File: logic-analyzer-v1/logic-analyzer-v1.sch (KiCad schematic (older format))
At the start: 0 parts

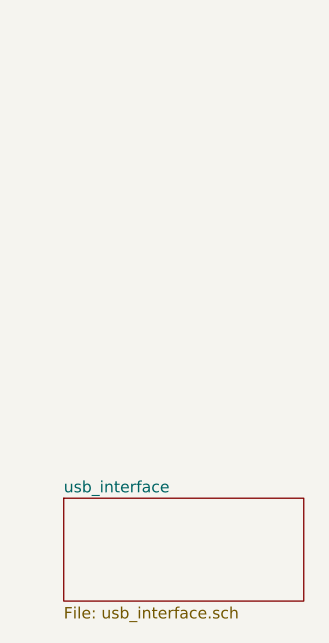
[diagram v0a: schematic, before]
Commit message: MOD usb-interface - review and minor fixes
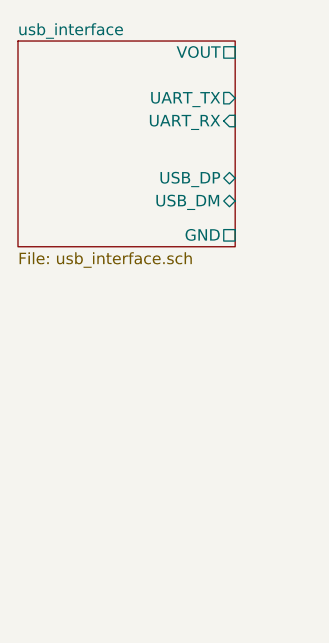
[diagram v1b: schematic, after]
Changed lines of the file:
@@
 $EndDescr
 $Sheet
-S 1350 5150 1050 450
+S 1150 3150 950  900
 U 5F08ED8D
 F0 "usb_interface" 50
 F1 "usb_interface.sch" 50
+F2 "UART_TX" O R 2100 3400 50
+F3 "UART_RX" I R 2100 3500 50
+F4 "VOUT" U R 2100 3200 50
+F5 "GND" U R 2100 4000 50
+F6 "USB_DP" B R 2100 3750 50
+F7 "USB_DM" B R 2100 3850 50
 $EndSheet
 $EndSCHEMATC

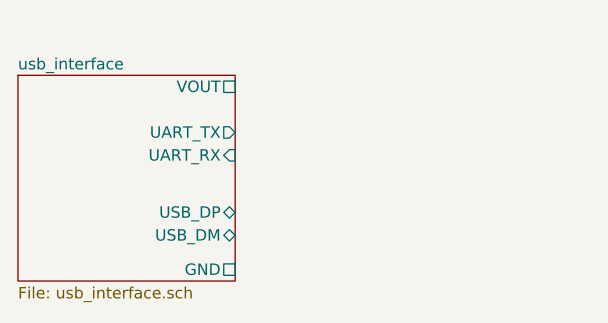
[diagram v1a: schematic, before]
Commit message: modify mcu sheet -> adding front end
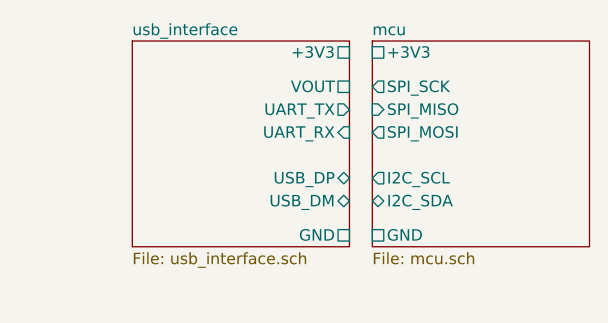
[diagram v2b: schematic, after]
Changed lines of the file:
@@
 $Descr A4 11693 8268
 encoding utf-8
-Sheet 1 2
+Sheet 1 3
 Title ""
 Date ""
@@
 $EndDescr
 $Sheet
-S 1150 3150 950  900
+S 1650 3000 950  900
 U 5F08ED8D
 F0 "usb_interface" 50
 F1 "usb_interface.sch" 50
-F2 "UART_TX" O R 2100 3400 50
-F3 "UART_RX" I R 2100 3500 50
-F4 "VOUT" U R 2100 3200 50
-F5 "GND" U R 2100 4000 50
-F6 "USB_DP" B R 2100 3750 50
-F7 "USB_DM" B R 2100 3850 50
+F2 "UART_TX" O R 2600 3300 50
+F3 "UART_RX" I R 2600 3400 50
+F4 "VOUT" U R 2600 3200 50
+F5 "GND" U R 2600 3850 50
+F6 "USB_DP" B R 2600 3600 50
+F7 "USB_DM" B R 2600 3700 50
+F8 "+3V3" U R 2600 3050 50
+$EndSheet
+$Sheet
+S 2700 3000 950  900
+U 5F19654C
+F0 "mcu" 50
+F1 "mcu.sch" 50
+F2 "I2C_SCL" O L 2700 3600 50
+F3 "I2C_SDA" B L 2700 3700 50
+F4 "SPI_MOSI" O L 2700 3400 50
+F5 "SPI_MISO" I L 2700 3300 50
+F6 "SPI_SCK" O L 2700 3200 50
+F7 "+3V3" U L 2700 3050 50
+F8 "GND" U L 2700 3850 50
 $EndSheet
 $EndSCHEMATC

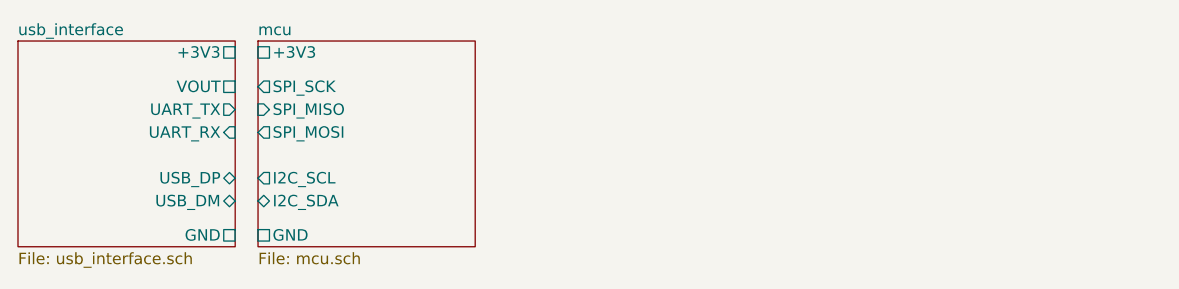
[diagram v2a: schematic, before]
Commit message: MOD usb power nets fix, mcu fixes
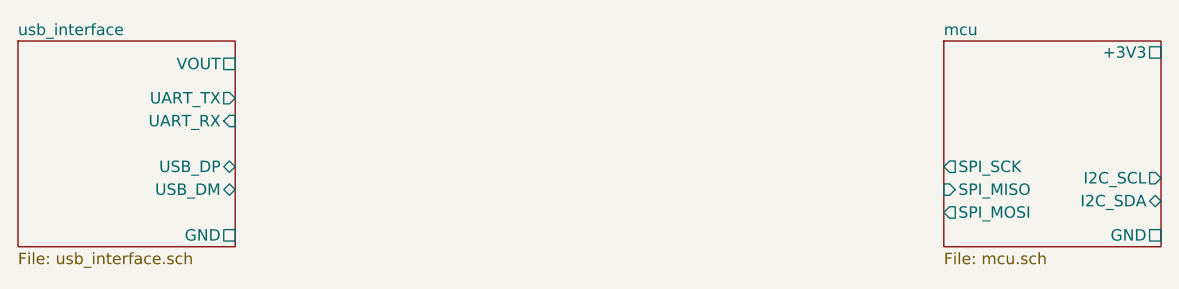
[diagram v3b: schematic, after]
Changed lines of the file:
@@
 F0 "usb_interface" 50
 F1 "usb_interface.sch" 50
-F2 "UART_TX" O R 2600 3300 50
-F3 "UART_RX" I R 2600 3400 50
-F4 "VOUT" U R 2600 3200 50
+F2 "UART_TX" O R 2600 3250 50
+F3 "UART_RX" I R 2600 3350 50
+F4 "VOUT" U R 2600 3100 50
 F5 "GND" U R 2600 3850 50
-F6 "USB_DP" B R 2600 3600 50
-F7 "USB_DM" B R 2600 3700 50
-F8 "+3V3" U R 2600 3050 50
+F6 "USB_DP" B R 2600 3550 50
+F7 "USB_DM" B R 2600 3650 50
 $EndSheet
 $Sheet
-S 2700 3000 950  900
+S 5700 3000 950  900
 U 5F19654C
 F0 "mcu" 50
 F1 "mcu.sch" 50
-F2 "I2C_SCL" O L 2700 3600 50
-F3 "I2C_SDA" B L 2700 3700 50
-F4 "SPI_MOSI" O L 2700 3400 50
-F5 "SPI_MISO" I L 2700 3300 50
-F6 "SPI_SCK" O L 2700 3200 50
-F7 "+3V3" U L 2700 3050 50
-F8 "GND" U L 2700 3850 50
+F2 "I2C_SCL" O R 6650 3600 50
+F3 "I2C_SDA" B R 6650 3700 50
+F4 "SPI_MOSI" O L 5700 3750 50
+F5 "SPI_MISO" I L 5700 3650 50
+F6 "SPI_SCK" O L 5700 3550 50
+F7 "+3V3" U R 6650 3050 50
+F8 "GND" U R 6650 3850 50
 $EndSheet
 $EndSCHEMATC

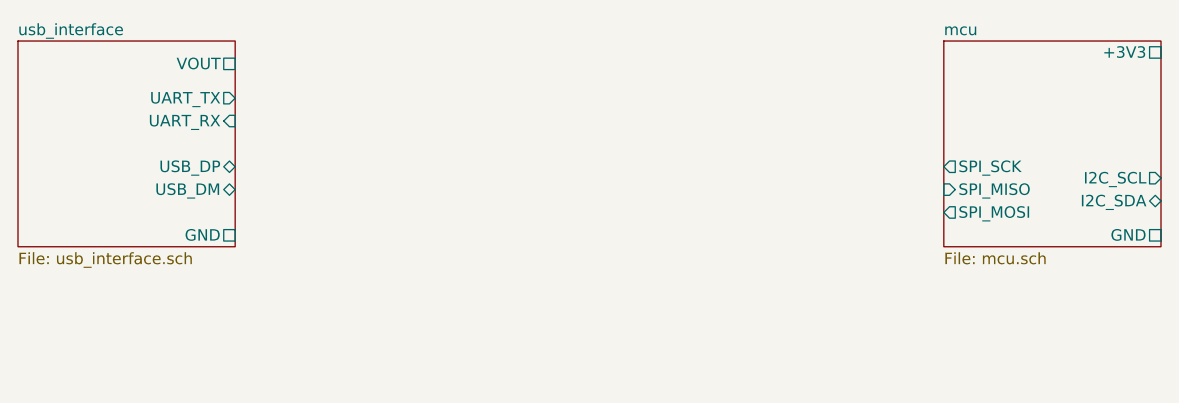
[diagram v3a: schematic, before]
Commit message: adding gpio pins, usb pins, usart pins
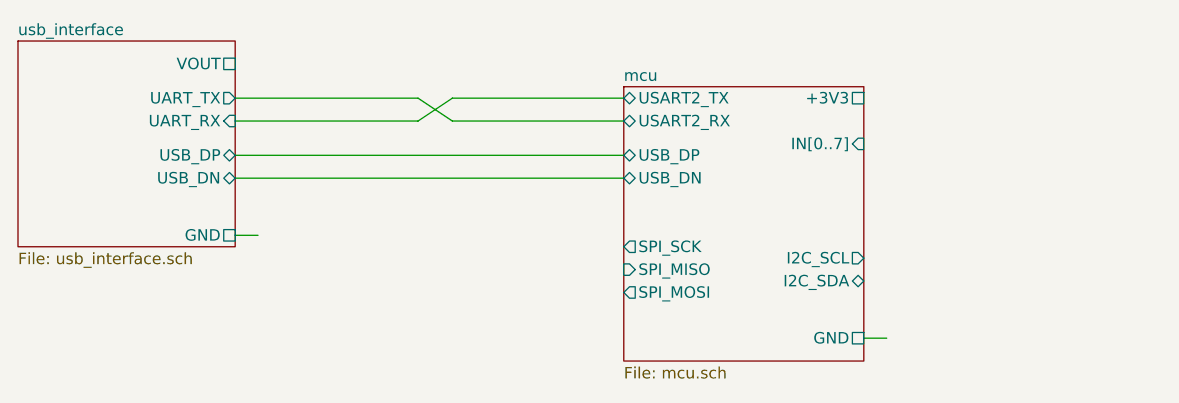
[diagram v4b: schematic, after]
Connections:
- wire segments 0 -> 10
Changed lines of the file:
@@
 F4 "VOUT" U R 2600 3100 50
 F5 "GND" U R 2600 3850 50
-F6 "USB_DP" B R 2600 3550 50
-F7 "USB_DM" B R 2600 3650 50
+F6 "USB_DP" B R 2600 3500 50
+F7 "USB_DN" B R 2600 3600 50
 $EndSheet
 $Sheet
-S 5700 3000 950  900
+S 4300 3200 1050 1200
 U 5F19654C
 F0 "mcu" 50
 F1 "mcu.sch" 50
-F2 "I2C_SCL" O R 6650 3600 50
-F3 "I2C_SDA" B R 6650 3700 50
-F4 "SPI_MOSI" O L 5700 3750 50
-F5 "SPI_MISO" I L 5700 3650 50
-F6 "SPI_SCK" O L 5700 3550 50
-F7 "+3V3" U R 6650 3050 50
-F8 "GND" U R 6650 3850 50
+F2 "I2C_SCL" O R 5350 3950 50
+F3 "I2C_SDA" B R 5350 4050 50
+F4 "SPI_MOSI" O L 4300 4100 50
+F5 "SPI_MISO" I L 4300 4000 50
+F6 "SPI_SCK" O L 4300 3900 50
+F7 "+3V3" U R 5350 3250 50
+F8 "GND" U R 5350 4300 50
+F9 "IN[0..7]" I R 5350 3450 50
+F10 "USB_DN" B L 4300 3600 50
+F11 "USB_DP" B L 4300 3500 50
+F12 "USART2_TX" B L 4300 3250 50
+F13 "USART2_RX" B L 4300 3350 50
 $EndSheet
+Wire Wire Line
+	2600 3250 3400 3250
+Wire Wire Line
+	4300 3350 3550 3350
+Wire Wire Line
+	3550 3350 3400 3250
+Wire Wire Line
+	4300 3250 3550 3250
+Wire Wire Line
+	3550 3250 3400 3350
+Wire Wire Line
+	3400 3350 2600 3350
+Wire Wire Line
+	2600 3500 4300 3500
+Wire Wire Line
+	4300 3600 2600 3600
+Wire Wire Line
+	5350 4300 5450 4300
+Wire Wire Line
+	2700 3850 2600 3850
 $EndSCHEMATC

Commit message: update 03.2021
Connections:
- wire segments 10 -> 27
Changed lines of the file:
@@
 $Descr A4 11693 8268
 encoding utf-8
-Sheet 1 3
+Sheet 1 6
 Title ""
 Date ""
@@
 F7 "USB_DN" B R 2600 3600 50
 $EndSheet
-$Sheet
-S 4300 3200 1050 1200
-U 5F19654C
-F0 "mcu" 50
-F1 "mcu.sch" 50
-F2 "I2C_SCL" O R 5350 3950 50
-F3 "I2C_SDA" B R 5350 4050 50
-F4 "SPI_MOSI" O L 4300 4100 50
-F5 "SPI_MISO" I L 4300 4000 50
-F6 "SPI_SCK" O L 4300 3900 50
-F7 "+3V3" U R 5350 3250 50
-F8 "GND" U R 5350 4300 50
-F9 "IN[0..7]" I R 5350 3450 50
-F10 "USB_DN" B L 4300 3600 50
-F11 "USB_DP" B L 4300 3500 50
-F12 "USART2_TX" B L 4300 3250 50
-F13 "USART2_RX" B L 4300 3350 50
-$EndSheet
 Wire Wire Line
 	2600 3250 3400 3250
@@
 Wire Wire Line
 	2700 3850 2600 3850
+$Sheet
+S 5950 3200 1100 1200
+U 5FDA887A
+F0 "frontend" 50
+F1 "frontend.sch" 50
+F2 "GND" U L 5950 4300 50
+F3 "I2C_SCL" I L 5950 3950 50
+F4 "I2C_SDA" B L 5950 4050 50
+$EndSheet
+Wire Wire Line
+	5950 3950 5350 3950
+Wire Wire Line
+	5350 4050 5950 4050
+$Sheet
+S 1800 4400 800  950
+U 5FDBE2FD
+F0 "memory" 50
+F1 "memory.sch" 50
+F2 "SPI_MOSI" I R 2600 4850 50
+F3 "SPI_MISO" O R 2600 4750 50
+F4 "SPI_SCK" I R 2600 4650 50
+F5 "SPI_CS_0" I R 2600 5050 50
+F6 "SPI_CS_1" I R 2600 5150 50
+F7 "GND" U R 2600 5300 50
+F8 "+3V3" U R 2600 4450 50
+$EndSheet
+$Sheet
+S 4300 3200 1050 1200
+U 5F19654C
+F0 "mcu" 50
+F1 "mcu.sch" 50
+F2 "I2C_SCL" O R 5350 3950 50
+F3 "I2C_SDA" B R 5350 4050 50
+F4 "SPI_MOSI" O L 4300 4000 50
+F5 "SPI_MISO" I L 4300 3900 50
+F6 "SPI_SCK" O L 4300 3800 50
+F7 "+3V3" U R 5350 3250 50
+F8 "GND" U R 5350 4300 50
+F9 "IN[0..7]" I R 5350 3450 50
+F10 "USB_DN" B L 4300 3600 50
+F11 "USB_DP" B L 4300 3500 50
+F12 "USART2_TX" B L 4300 3250 50
+F13 "USART2_RX" B L 4300 3350 50
+F14 "SPI_CS_0" O L 4300 4200 50
+F15 "SPI_CS_1" O L 4300 4300 50
+$EndSheet
+Wire Wire Line
+	4300 3800 3400 3800
+Wire Wire Line
+	3400 3800 3400 4650
+Wire Wire Line
+	3400 4650 2600 4650
+Wire Wire Line
+	4300 3900 3500 3900
+Wire Wire Line
+	3500 3900 3500 4750
+Wire Wire Line
+	3500 4750 2600 4750
+Wire Wire Line
+	4300 4000 3600 4000
+Wire Wire Line
+	3600 4000 3600 4850
+Wire Wire Line
+	3600 4850 2600 4850
+Wire Wire Line
+	4300 4200 3800 4200
+Wire Wire Line
+	3800 4200 3800 5050
+Wire Wire Line
+	3800 5050 2600 5050
+Wire Wire Line
+	4300 4300 3900 4300
+Wire Wire Line
+	3900 4300 3900 5150
+Wire Wire Line
+	3900 5150 2600 5150
 $EndSCHEMATC

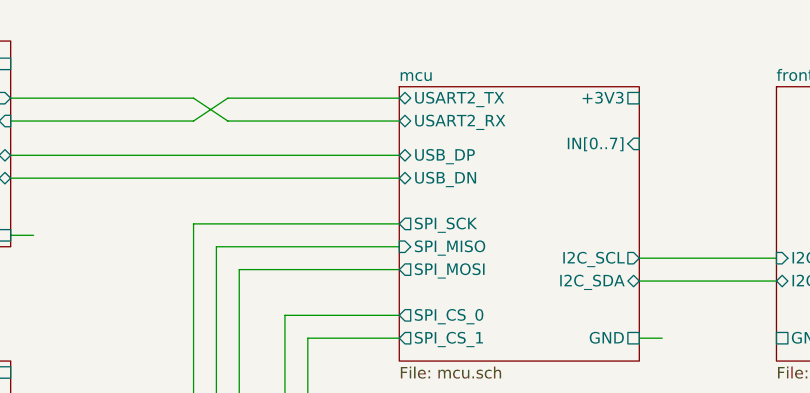
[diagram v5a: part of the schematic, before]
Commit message: MOD uart port direction, minor cosmetic changes
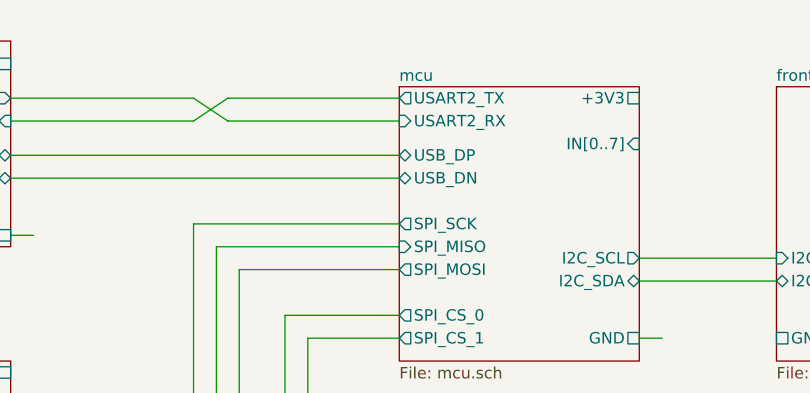
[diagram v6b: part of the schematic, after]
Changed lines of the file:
@@
 $Descr A4 11693 8268
 encoding utf-8
-Sheet 1 6
+Sheet 1 8
 Title ""
 Date ""
@@
 F10 "USB_DN" B L 4300 3600 50
 F11 "USB_DP" B L 4300 3500 50
-F12 "USART2_TX" B L 4300 3250 50
-F13 "USART2_RX" B L 4300 3350 50
+F12 "USART2_TX" O L 4300 3250 50
+F13 "USART2_RX" I L 4300 3350 50
 F14 "SPI_CS_0" O L 4300 4200 50
 F15 "SPI_CS_1" O L 4300 4300 50

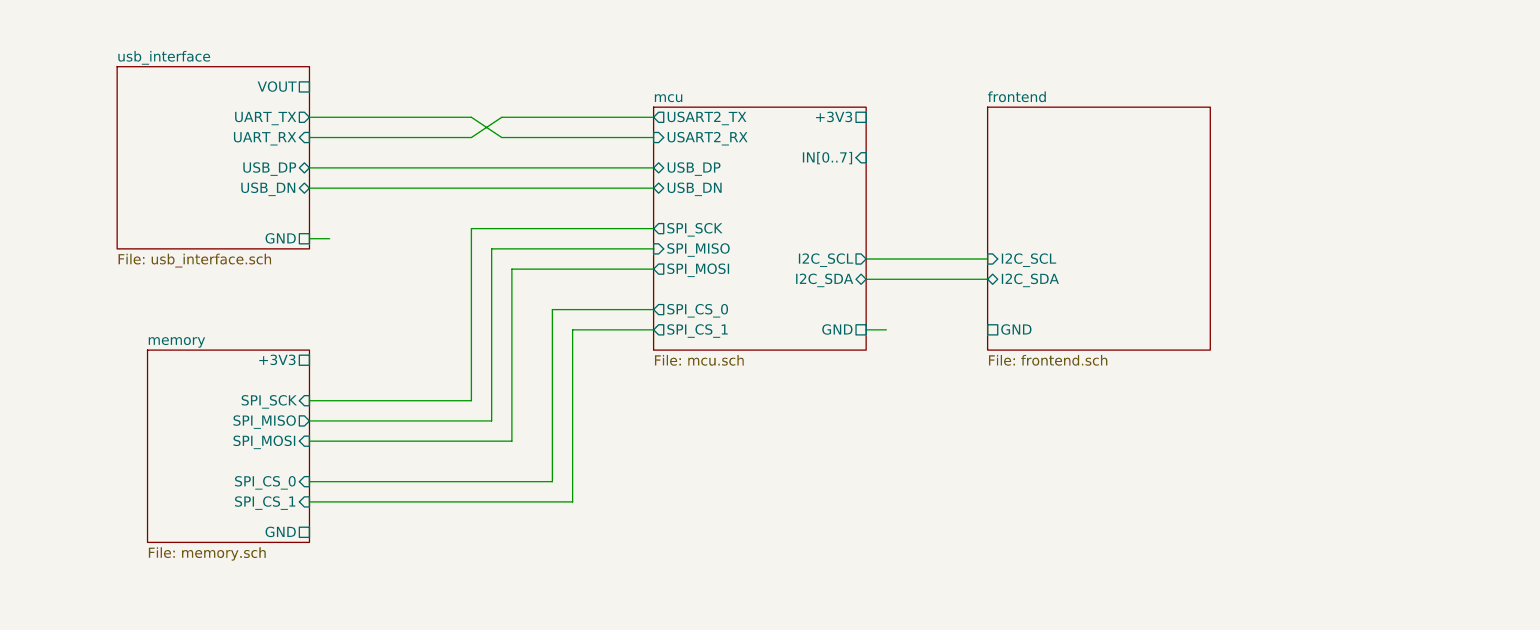
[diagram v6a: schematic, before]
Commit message: changing sram blocks from new library
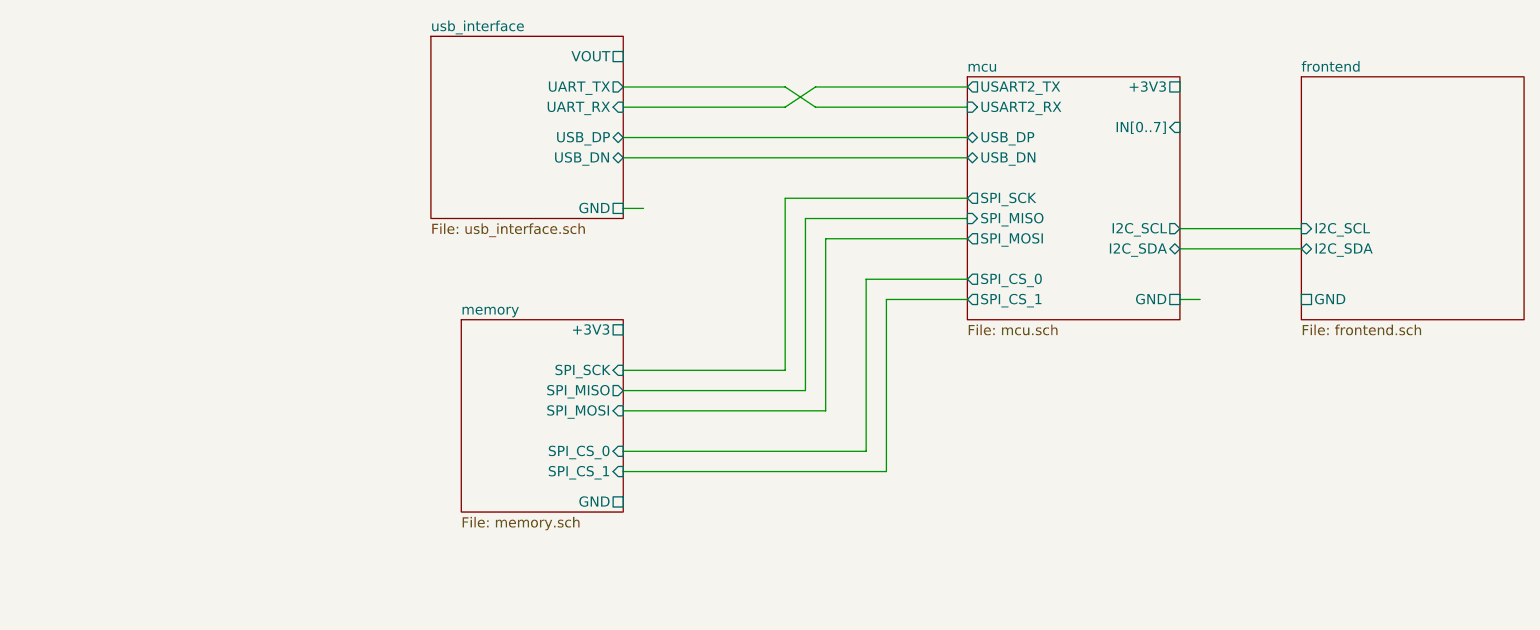
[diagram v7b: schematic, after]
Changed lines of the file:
@@
 $EndDescr
 $Sheet
-S 1650 3000 950  900
+S 3200 2850 950  900
 U 5F08ED8D
 F0 "usb_interface" 50
 F1 "usb_interface.sch" 50
-F2 "UART_TX" O R 2600 3250 50
-F3 "UART_RX" I R 2600 3350 50
-F4 "VOUT" U R 2600 3100 50
-F5 "GND" U R 2600 3850 50
-F6 "USB_DP" B R 2600 3500 50
-F7 "USB_DN" B R 2600 3600 50
+F2 "UART_TX" O R 4150 3100 50
+F3 "UART_RX" I R 4150 3200 50
+F4 "VOUT" U R 4150 2950 50
+F5 "GND" U R 4150 3700 50
+F6 "USB_DP" B R 4150 3350 50
+F7 "USB_DN" B R 4150 3450 50
 $EndSheet
 Wire Wire Line
-	2600 3250 3400 3250
+	4150 3100 4950 3100
 Wire Wire Line
-	4300 3350 3550 3350
+	5850 3200 5100 3200
 Wire Wire Line
-	3550 3350 3400 3250
+	5100 3200 4950 3100
 Wire Wire Line
-	4300 3250 3550 3250
+	5850 3100 5100 3100
 Wire Wire Line
-	3550 3250 3400 3350
+	5100 3100 4950 3200
 Wire Wire Line
-	3400 3350 2600 3350
+	4950 3200 4150 3200
 Wire Wire Line
-	2600 3500 4300 3500
+	4150 3350 5850 3350
 Wire Wire Line
-	4300 3600 2600 3600
+	5850 3450 4150 3450
 Wire Wire Line
-	5350 4300 5450 4300
+	6900 4150 7000 4150
 Wire Wire Line
-	2700 3850 2600 3850
+	4250 3700 4150 3700
 $Sheet
-S 5950 3200 1100 1200
+S 7500 3050 1100 1200
 U 5FDA887A
 F0 "frontend" 50
 F1 "frontend.sch" 50
-F2 "GND" U L 5950 4300 50
-F3 "I2C_SCL" I L 5950 3950 50
-F4 "I2C_SDA" B L 5950 4050 50
+F2 "GND" U L 7500 4150 50
+F3 "I2C_SCL" I L 7500 3800 50
+F4 "I2C_SDA" B L 7500 3900 50
 $EndSheet
 Wire Wire Line
-	5950 3950 5350 3950
+	7500 3800 6900 3800
 Wire Wire Line
-	5350 4050 5950 4050
+	6900 3900 7500 3900
 $Sheet
-S 1800 4400 800  950
+S 3350 4250 800  950
 U 5FDBE2FD
 F0 "memory" 50
 F1 "memory.sch" 50
-F2 "SPI_MOSI" I R 2600 4850 50
-F3 "SPI_MISO" O R 2600 4750 50
-F4 "SPI_SCK" I R 2600 4650 50
-F5 "SPI_CS_0" I R 2600 5050 50
-F6 "SPI_CS_1" I R 2600 5150 50
-F7 "GND" U R 2600 5300 50
-F8 "+3V3" U R 2600 4450 50
+F2 "SPI_MOSI" I R 4150 4700 50
+F3 "SPI_MISO" O R 4150 4600 50
+F4 "SPI_SCK" I R 4150 4500 50
+F5 "SPI_CS_0" I R 4150 4900 50
+F6 "SPI_CS_1" I R 4150 5000 50
+F7 "GND" U R 4150 5150 50
+F8 "+3V3" U R 4150 4300 50
 $EndSheet
 $Sheet
-S 4300 3200 1050 1200
+S 5850 3050 1050 1200
 U 5F19654C
 F0 "mcu" 50
 F1 "mcu.sch" 50
-F2 "I2C_SCL" O R 5350 3950 50
-F3 "I2C_SDA" B R 5350 4050 50
-F4 "SPI_MOSI" O L 4300 4000 50
-F5 "SPI_MISO" I L 4300 3900 50
-F6 "SPI_SCK" O L 4300 3800 50
-F7 "+3V3" U R 5350 3250 50
-F8 "GND" U R 5350 4300 50
-F9 "IN[0..7]" I R 5350 3450 50
-F10 "USB_DN" B L 4300 3600 50
-F11 "USB_DP" B L 4300 3500 50
-F12 "USART2_TX" O L 4300 3250 50
-F13 "USART2_RX" I L 4300 3350 50
-F14 "SPI_CS_0" O L 4300 4200 50
-F15 "SPI_CS_1" O L 4300 4300 50
+F2 "I2C_SCL" O R 6900 3800 50
+F3 "I2C_SDA" B R 6900 3900 50
+F4 "SPI_MOSI" O L 5850 3850 50
+F5 "SPI_MISO" I L 5850 3750 50
+F6 "SPI_SCK" O L 5850 3650 50
+F7 "+3V3" U R 6900 3100 50
+F8 "GND" U R 6900 4150 50
+F9 "IN[0..7]" I R 6900 3300 50
+F10 "USB_DN" B L 5850 3450 50
+F11 "USB_DP" B L 5850 3350 50
+F12 "USART2_TX" O L 5850 3100 50
+F13 "USART2_RX" I L 5850 3200 50
+F14 "SPI_CS_0" O L 5850 4050 50
+F15 "SPI_CS_1" O L 5850 4150 50
 $EndSheet
 Wire Wire Line
-	4300 3800 3400 3800
+	5850 3650 4950 3650
 Wire Wire Line
-	3400 3800 3400 4650
+	4950 3650 4950 4500
 Wire Wire Line
-	3400 4650 2600 4650
+	4950 4500 4150 4500
 Wire Wire Line
-	4300 3900 3500 3900
+	5850 3750 5050 3750
 Wire Wire Line
-	3500 3900 3500 4750
+	5050 3750 5050 4600
 Wire Wire Line
-	3500 4750 2600 4750
+	5050 4600 4150 4600
 Wire Wire Line
-	4300 4000 3600 4000
+	5850 3850 5150 3850
 Wire Wire Line
-	3600 4000 3600 4850
+	5150 3850 5150 4700
 Wire Wire Line
-	3600 4850 2600 4850
+	5150 4700 4150 4700
 Wire Wire Line
-	4300 4200 3800 4200
+	5850 4050 5350 4050
 Wire Wire Line
-	3800 4200 3800 5050
+	5350 4050 5350 4900
 Wire Wire Line
-	3800 5050 2600 5050
+	5350 4900 4150 4900
 Wire Wire Line
-	4300 4300 3900 4300
+	5850 4150 5450 4150
 Wire Wire Line
-	3900 4300 3900 5150
+	5450 4150 5450 5000
 Wire Wire Line
-	3900 5150 2600 5150
+	5450 5000 4150 5000
 $EndSCHEMATC
